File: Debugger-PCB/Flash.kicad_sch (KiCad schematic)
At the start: 2 parts, among them U7 W25Q32JVSS

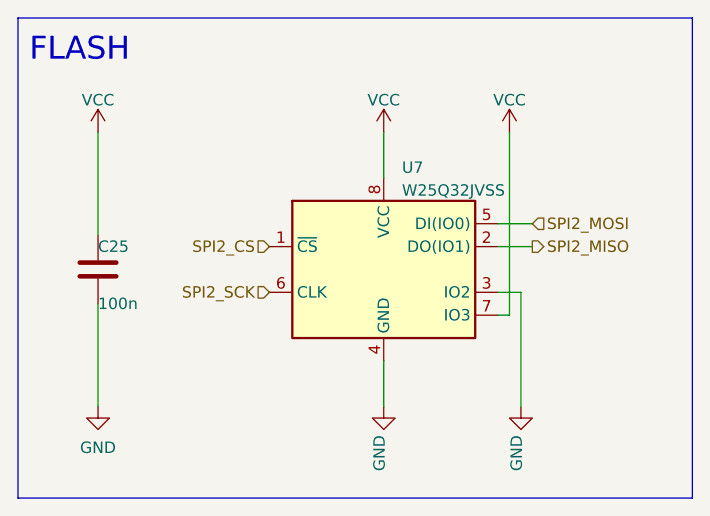
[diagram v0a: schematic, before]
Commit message: change the file name debugger-code into debugger_code_f103. Change the stm32f103rct6 into stm32f407vet6. Add file debugger_code_f407
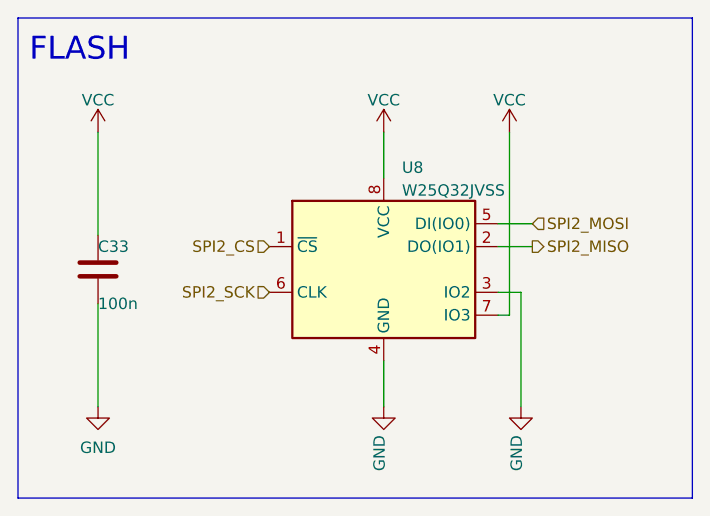
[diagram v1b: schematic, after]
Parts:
- renumbered C25 to C33, U7 to U8
